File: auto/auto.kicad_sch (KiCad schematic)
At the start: 25 parts, among them J1 BATERIAS_PC, J2 BATERIA_AUTO, J3 servo, J4 BOCINA, Q1 2N3904, Q2 2N3904, SW1 SW_DPST_x2, SW2 SW1, SW3 SW_DPST_x2, SW4 SW_DPST_x2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

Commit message: esquematico(falta agregar fusible 1 / 2 A)
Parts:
- SW1: footprint (none) -> Button_Switch_THT:SW_DIP_SPSTx01_Slide_6.7x4.1mm_W7.62mm_P2.54mm_LowProfile
- SW2, SW3, SW4: footprint (none) -> Button_Switch_THT:SW_PUSH-12mm_Wuerth-430476085716
- U1: footprint (none) -> GY-NEO6MV2:GY-NEO6MV2
- U6: footprint (none) -> Package_TO_SOT_THT:TO-220-3_Vertical
- U8: footprint (none) -> LORA:SHIELD XL1278
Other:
- note added: "FUSE 2A"
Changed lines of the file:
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@@
 		(company "Joaquin Della Torre ")
 	)
+	(text "FUSE 2A"
+		(exclude_from_sim no)
+		(at 36.068 149.86 0)
+		(effects
+			(font
+				(size 1.27 1.27)
+			)
+		)
+	)
 	(junction
 		(at 142.24 142.24)
@@
 			)
 		)
-		(property "Footprint" ""
+		(property "Footprint" "Package_TO_SOT_THT:TO-220-3_Vertical"
 			(at 60.325 146.05 0)
 			(effects
@@
 			)
 		)
-		(property "Footprint" ""
+		(property "Footprint" "Button_Switch_THT:SW_PUSH-12mm_Wuerth-430476085716"
 			(at 142.24 177.8 0)
 			(effects
@@
 			)
 		)
-		(property "Footprint" ""
+		(property "Footprint" "GY-NEO6MV2:GY-NEO6MV2"
 			(at 33.02 73.66 0)
 			(effects
@@
 			)
 		)
-		(property "Footprint" ""
+		(property "Footprint" "Button_Switch_THT:SW_PUSH-12mm_Wuerth-430476085716"
 			(at 142.24 170.18 0)
 			(effects
@@
 			)
 		)
-		(property "Footprint" ""
+		(property "Footprint" "Button_Switch_THT:SW_DIP_SPSTx01_Slide_6.7x4.1mm_W7.62mm_P2.54mm_LowProfile"
 			(at 34.29 142.24 0)
 			(effects
@@
 			)
 		)
-		(property "Footprint" ""
+		(property "Footprint" "Button_Switch_THT:SW_PUSH-12mm_Wuerth-430476085716"
 			(at 142.24 185.42 0)
 			(effects
@@
 			)
 		)
-		(property "Footprint" ""
+		(property "Footprint" "LORA:SHIELD XL1278"
 			(at 31.75 41.91 0)
 			(effects

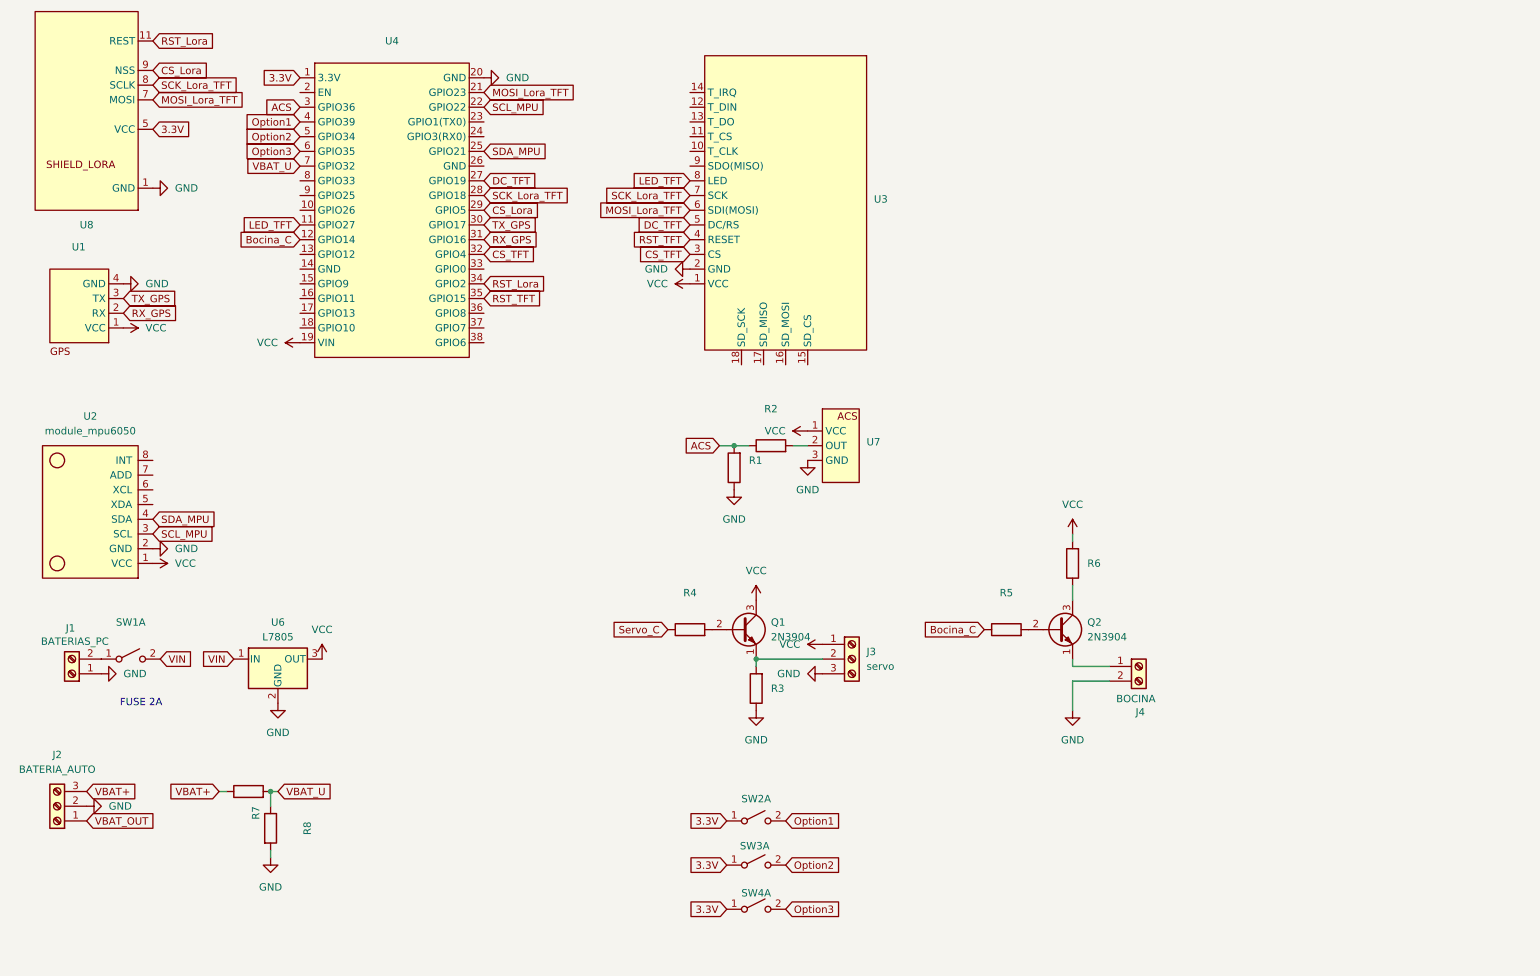
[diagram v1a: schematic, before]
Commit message: esquematico finalizado, PCB en proceso.
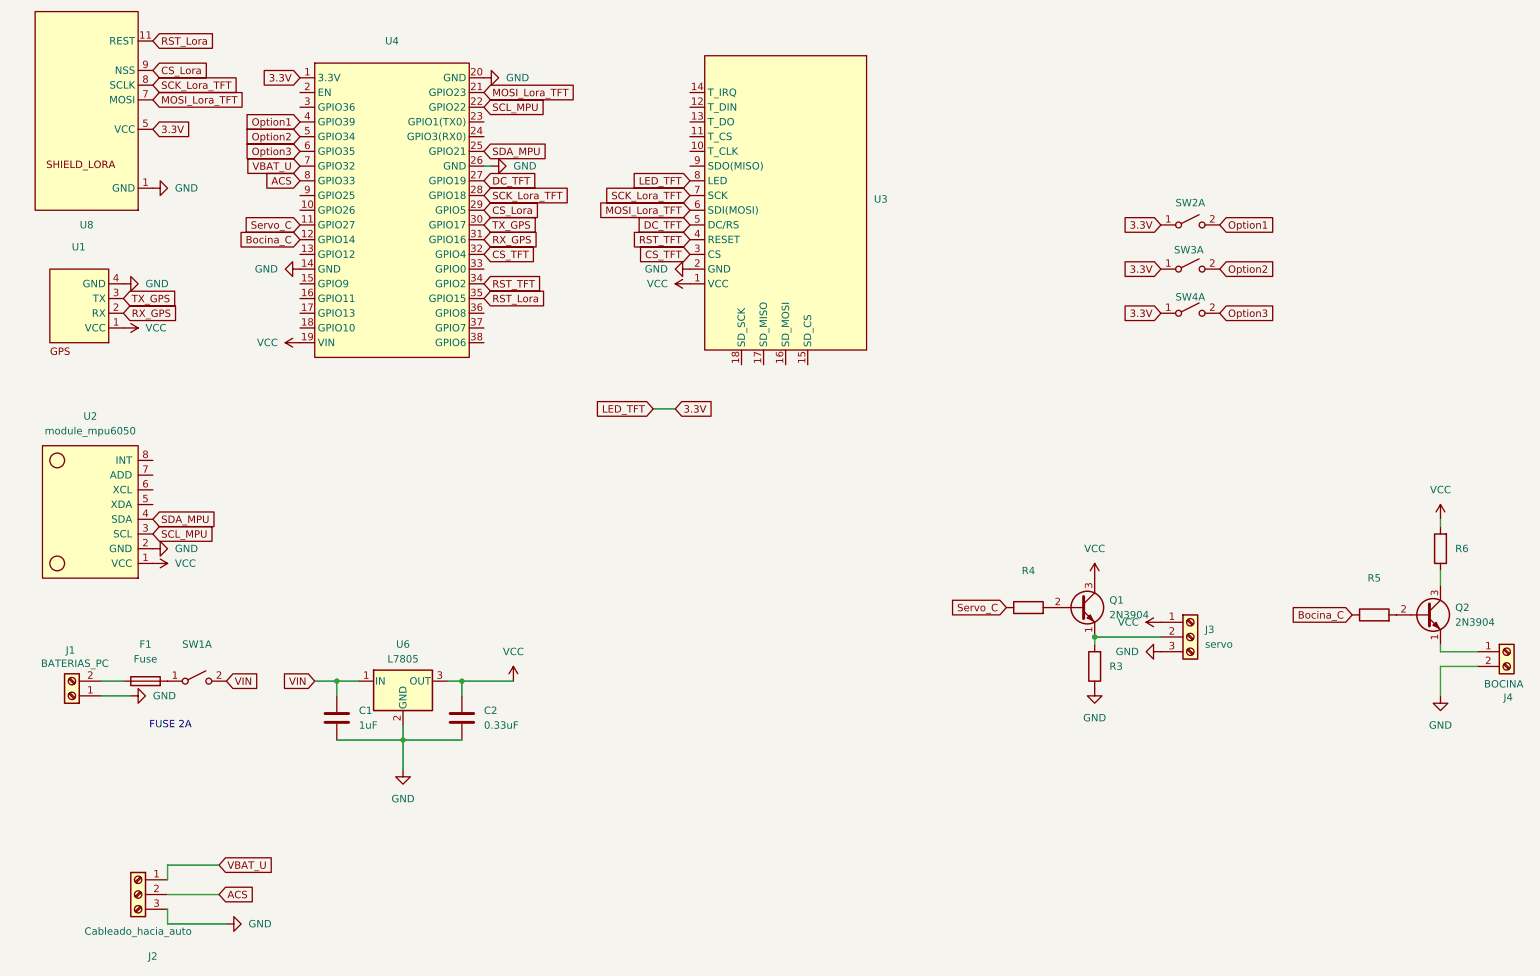
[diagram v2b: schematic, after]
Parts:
- removed R1, R7: 10K, Resistor_THT:R_Axial_DIN0204_L3.6mm_D1.6mm_P5.08mm_Horizontal, symbol Device:R
- removed R2, R8: 10k, Resistor_THT:R_Axial_DIN0204_L3.6mm_D1.6mm_P5.08mm_Horizontal, symbol Device:R
- removed U7: ~, Connector_PinHeader_2.54mm:PinHeader_1x03_P2.54mm_Vertical, symbol acs_module:ACS712
- added C1: 1uF, Resistor_THT:R_Axial_DIN0204_L3.6mm_D1.6mm_P5.08mm_Horizontal, symbol Device:C
- added C2: 0.33uF, Resistor_THT:R_Axial_DIN0204_L3.6mm_D1.6mm_P5.08mm_Horizontal, symbol Device:C
- added F1: Fuse, Fuse:Fuseholder_Clip-5x20mm_Littelfuse_445-030_Inline_P20.50x5.20mm_D1.30mm_Horizontal, symbol Device:Fuse
- J1: footprint Connector_PinHeader_2.54mm:PinHeader_1x02_P2.54mm_Vertical -> TerminalBlock:TerminalBlock_MaiXu_MX126-5.0-02P_1x02_P5.00mm
- J2: value BATERIA_AUTO -> Cableado_hacia_auto; footprint terminals_bateries:teminals_bateries -> TerminalBlock:TerminalBlock_MaiXu_MX126-5.0-03P_1x03_P5.00mm
- R4: footprint Resistor_THT:R_Axial_DIN0204_L3.6mm_D1.6mm_P5.08mm_Horizontal -> Resistor_THT:R_Axial_DIN0207_L6.3mm_D2.5mm_P10.16mm_Horizontal
- U2: footprint Connector_PinHeader_2.54mm:PinHeader_1x08_P2.54mm_Vertical -> MPU6050:module_MPU6050
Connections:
- net VBAT+ is gone; now on net GND: J2.3 (Pin_3)
- net VBAT_OUT is gone; now on net VBAT_U: J2.1 (Pin_1)
- net 3.3V: now also U3.8 (LED)
- net ACS: now also J2.2 (Pin_2), U4.8 (GPIO33); no longer U4.3 (GPIO36)
- net GND: now also U4.14 (GND), U4.26 (GND), C1.2, C2.2; no longer J2.2 (Pin_2)
- net RST_Lora: now also U4.35 (GPIO15); no longer U4.34 (GPIO2)
- net RST_TFT: now also U4.34 (GPIO2); no longer U4.35 (GPIO15)
- net Servo_C: now also U4.11 (GPIO27)
- net VCC: now also C2.1
- net VIN: now also C1.1
- net at J1.2 (Pin_2): now also F1.1; no longer SW1.1 (A)
- removed net LED_TFT: U3.8 (LED), U4.11 (GPIO27)
- new net: F1.2, SW1.1 (A)
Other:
- moved on the sheet: J1, J3, J4, Q1, Q2, R3, R4, R5, R6, SW1A, SW2A, SW3A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
